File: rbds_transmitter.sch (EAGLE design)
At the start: 137 parts, among them IC1 TS974, IC2 TS974, IC3 MAX1551, IC4 MAX2606, IC5 TPS61030, IC6 MCP4812, Q1 P-CH, Q2 P-Ch, Q3 P-Ch, U1 ATMEGA328, X1 HD44780LCD-1602, Y1 16Mhz

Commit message: final design tweaks for hardware descript
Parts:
- removed ANT2: (no value), discrete:ANTENNA
- removed IC4: MAX2606, maxim:MAX2606
- removed IC6: MCP4812, microchip:MCP4812
- removed ISP1: AVRISP-6, adafruit:AVRISP-6
- removed JP1: (no value), sparkfun:M03PTH
- removed JP3, JP4: M01PTH, sparkfun:M01PTH
- removed Y1: 16Mhz, sparkfun:RESONATORSMD
- added J2: AVRISP-6, adafruit:AVRISP-6
- added LCD1: HD44780LCD-1602, adafruit:HD44780LCD-1602
- added P1: (no value), sparkfun:M03PTH
- added TP2, TP3: M01PTH, sparkfun:M01PTH
- added U5: ATMEGA328, sparkfun:ATMEGA168
- added U7: MCP4812, microchip:MCP4812
- ANT1: value (none) -> ANT; device discrete:ANTENNA -> dipole_antenna:ANT
- C1: value 1nF -> 1uF
- C10, C11: value 1uF -> 10uF
- C12: value 0.1uF -> 10uF
- C13, C14, C15: value 10uF -> 4.7uF
- C16: value 100pF -> 0.1uF
- C18, C23: value 0.1uF -> 4.7uF
- C21: value 4.7uF -> 1nF
- C22, C24: value 4.7uF -> 0.1uF
- C26, C27: value 4.7uF -> 1.5nF
- C28: value 4.7uF -> 1.2nF
- C29: value 1.396nF -> 1.2nF
- C30, C31: value 1.396nF -> 3.9nF
- C32, C33: value 1.34nF -> 3nF
- C34, C35: value 1.34nF -> 1nF
- C36: value 3.06nF -> 1uF
- C37: value 3.06nF -> 4.7uF
- C38, C39: value 3.06nF -> 1.5nF
- C40: value 100pF -> 1.2nF
- C41: value 4.188nF -> 1.2nF
- C42, C43: value 4.188nF -> 3.9nF
- C44: value 4.188nF -> 3nF
- C45: value 1.396nF -> 3nF
- L1: device rcl:L-USL1812 -> resistor:L-USL1812
- L2: value (none) -> 485nH; device resistor:L-USL1812 -> resistor:L-USL3216C
- L3: value (none) -> 10mH
- L4: value 485nH -> 6.8uH; device resistor:L-USL1812 -> rcl:L-USL1812
- R1: value 332 -> 1k
- R10, R11, R12, R14: value 2k -> 10k
- R13: value 2k -> 200
- R15: value 2k -> (none)
- R16, R17: value 2k -> 100k
- R18, R19: value 1k -> 100k
- R2, R8: value 10k -> 1k
- R20: value (none) -> 100k
- R21: value 200 -> 100k
- R24: value 100k -> 1.8M
- R25, R26, R27: value 10k -> 100k
- R28: value 10k -> 390k
- R29: value 1k -> 200k
- R3: value 10k -> 200
- R30: value 2k -> 100
- R31, R32, R33, R34, R35: value 2k -> 100k; device adafruit:R-US_R1206 -> rcl:R-TRIMM4G/J
- R36: value 2k -> 1.95M
- R37: value 1.8M -> 2k
- R38: value 390k -> 2k
- R39: value 200k -> 2k
- R40, R41, R42, R43, R44, R46, R47: value 100k -> 2k
- R45: value 100k -> 100
- R48: value 1.95M -> 2k
- R49, R50, R51, R52, R53: value 100k -> 2k; device rcl:R-TRIMM4G/J -> adafruit:R-US_R1206
- R5: value 200 -> 10k
- R9: value 2k -> 332
- U1: value ATMEGA328 -> MAX2606; device sparkfun:ATMEGA168 -> maxim:MAX2606
- X1: value HD44780LCD-1602 -> 16Mhz; device adafruit:HD44780LCD-1602 -> sparkfun:RESONATORSMD
- renumbered CN1 to J1, IC1 to U2, IC2 to U3, IC3 to U4, IC5 to U6, JP10 to TP1, JP11 to P2, JP2 to B1, JP5 to TP4, JP6 to TP5, JP7 to TP6, JP8 to TP7, JP9 to TP8, TR1 to T2, TR2 to T1
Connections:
- removed net N$15: R38.2, R48.1, U6.LBI
- new net N$27: R14.2, U7.A
- new net U7: R28.2, R36.1, U6.LBI
- net !DAC_CS: now also R10.2, U5.PD5(T1), U7.!CS; no longer IC6.!CS, R2.2, U1.PD5(T1)
- net !DAC_LATCH: now also R11.1, U5.PD6(AIN0), U7.!LDAC; no longer IC6.!LDAC, R3.1, U1.PD6(AIN0)
- net !ISP-RST: now also J2.RST, R4.1, U5.PC6(/RESET); no longer ISP1.RST, R25.1, U1.PC6(/RESET)
- net !LCD_EN: now also R17.1, U5.PD2(INT0); no longer R41.1, U1.PD2(INT0)
- net !TX_EN: now also R20.1, U5.PD1(TXD); no longer R44.1, U1.PD1(TXD)
- net +5V: now also C15.1, C20.1, C24.1, C3.1, J2.VCC, P1.3, R10.1, R16.2, R17.2, R20.2, R24.2, R4.2, U5.AREF, U5.AVCC, U5.VCC@1, U5.VCC@2; no longer C12.1, C18.1, C2.1, C28.1, ISP1.VCC, JP1.3, R2.1, R25.2, R37.2, R40.2, R41.2, R44.2, U1.AREF, U1.AVCC, U1.VCC@1, U1.VCC@2
- net AGND: now also C22.2, U5.AGND; no longer C12.2, U1.AGND
- net BPSK: now also R13.2, TP3.1; no longer JP4.1, R5.2
- net CARRIER: now also R38.2, U5.PB1(OC1A); no longer R30.2, U1.PB1(OC1A)
- net FREQUENCY: now also R21.1, TP2.1; no longer JP3.1, R45.1
- net GND: now also C13.2, C14.2, C15.2, C16.2, C3.2, C40.2, J2.GND, L2.1, LCD1.RW, LCD1.VSS, P1.1, R11.2, R12.1, R18.2, R22.2, R26.2, R28.1, R29.1, R9.1, U1.GND, U5.GND@1, U5.GND@2, U7.VSS, X1.2; no longer C1.2, C11.2, C21.2, C22.2, C34.2, C5.2, IC4.GND, IC6.VSS, ISP1.GND, JP1.1, L4.1, R1.1, R3.2, R38.1, R39.1, R4.1, R42.2, R46.2, R47.2, U1.GND@1, U1.GND@2, X1.RW, X1.VSS, Y1.2
- net ISP-MISO: now also J2.MISO, R7.2, U5.PB4(MISO); no longer ISP1.MISO, R28.2, U1.PB4(MISO)
- net ISP-MOSI: now also J2.MOSI, R6.2, U5.PB3(MOSI/OC2); no longer ISP1.MOSI, R27.2, U1.PB3(MOSI/OC2)
- net ISP-SCK: now also J2.SCK, R5.2, U5.PB5(SCK); no longer ISP1.SCK, R26.2, U1.PB5(SCK)
- net LCD0: now also LCD1.RS, U5.PC4(ADC4/SDA); no longer U1.PC4(ADC4/SDA), X1.RS
- net LCD1: now also LCD1.E, U5.PC5(ADC5/SCL); no longer U1.PC5(ADC5/SCL), X1.E
- net LCD2: now also LCD1.DB4, U5.PC0(ADC0); no longer U1.PC0(ADC0), X1.DB4
- net LCD3: now also LCD1.DB5, U5.PC1(ADC1); no longer U1.PC1(ADC1), X1.DB5
- net LCD4: now also LCD1.DB6, U5.PC2(ADC2); no longer U1.PC2(ADC2), X1.DB6
- net LCD5: now also LCD1.DB7, U5.PC3(ADC3); no longer U1.PC3(ADC3), X1.DB7
- net LOWBAT: now also R16.1, U5.PD4(XCK/T0); no longer R40.1, U1.PD4(XCK/T0)
- net MISO: now also R7.1; no longer R28.1
- net MOSI: now also R6.1, U7.SDI; no longer IC6.SDI, R27.1
- net N$1: now also C23.1, L1.2; no longer C17.1, L3.2
- net N$10: now also R15.2; no longer R20.2
- net N$11: now also C25.1, R15.1; no longer C19.1, R20.1
- net N$12: now also L4.2; no longer L1.2
- net N$17: now also R24.1, R29.2; no longer R37.1, R39.2
- net N$19: now also C12.2; no longer C15.2
- net N$2: now also U5.PB7(XTAL2/TOSC2), X1.3; no longer U1.PB7(XTAL2/TOSC2), Y1.3
- net N$20: now also C10.2; no longer C13.2
- net N$21: now also C17.1, L3.2; no longer C24.1, L2.2
- net N$22: now also R35.S; no longer R53.S
- net N$23: now also C5.1, R35.E; no longer C4.1, R53.E
- net N$24: now also L2.2, U1.IND; no longer IC4.IND, L4.2
- net N$25: now also C10.1, R13.1; no longer C13.1, R5.1
- net N$26: now also C12.1, R3.2; no longer C15.1, R21.2
- net N$28: now also U7.B; no longer IC6.B
- net N$33: now also C21.1, R30.2, U1.OUT+; no longer C40.1, IC4.OUT+, R7.2
- net N$35: now also C34.1, R45.2, U1.OUT-; no longer C16.1, IC4.OUT-, R8.2
- net N$39: now also ANT1.SIGNAL, C21.2; no longer ANT1.1, C40.2
- net N$4: now also U5.PB6(XTAL1/TOSC1), X1.1; no longer U1.PB6(XTAL1/TOSC1), Y1.1
- net N$42: now also C11.1; no longer C14.1
- net N$46: now also R12.2, R14.1; no longer IC6.A, R4.2, R6.1
- net N$5: now also C4.2, R18.1, R19.2, R35.A; no longer C3.2, R42.1, R43.2, R53.A
- net N$50: now also L4.1, R36.2; no longer L1.1, R48.2
- net N$52: now also ANT1.GND, C34.2; no longer ANT2.1, C16.2
- net N$54: now also L1.1; no longer L3.1
- net N$55: now also C27.1, R37.2, R38.1; no longer C29.1, R30.1, R31.2
- net N$59: now also C26.1, R37.1, R46.2; no longer C30.1, R31.1, R32.2
- net N$60: now also C28.1, R39.1, R48.2; no longer C33.1, R10.2, R9.1
- net N$61: now also C40.1, R48.1, R49.2; no longer C34.1, R10.1, R11.2
- net N$62: now also C41.1, R31.A, R49.1; no longer C35.1, R11.1, R49.A
- net N$63: now also C39.1, R34.A, R47.1; no longer C45.1, R36.1, R52.A
- net N$64: now also R31.S; no longer R49.S
- net N$65: now also R31.E; no longer R49.E
- net N$66: now also C2.1, R26.1, R27.2; no longer C11.1, R23.1, R24.2
- net N$67: now also C30.1, R41.1, R50.2; no longer C42.1, R12.1, R13.2
- net N$68: now also C42.1, R50.1, R51.2; no longer C43.1, R13.1, R14.2
- net N$69: now also C43.1, R32.A, R51.1; no longer C44.1, R14.1, R50.A
- net N$70: now also R32.S; no longer R50.S
- net N$71: now also R32.E; no longer R50.E
- net N$72: now also C32.1, R43.1, R52.2; no longer C37.1, R15.1, R16.2
- net N$73: now also C44.1, R52.1, R53.2; no longer C38.1, R16.1, R17.2
- net N$74: now also C45.1, R33.A, R53.1; no longer C39.1, R17.1, R51.A
- net N$75: now also R33.S; no longer R51.S
- net N$76: now also C1.1, R33.E; no longer C10.1, R51.E
- net N$77: now also R34.S; no longer R52.S
- net N$78: now also R1.2; no longer R18.2
- net N$79: now also R2.2; no longer R19.2
- net N$80: now also C1.2, R8.2; no longer C10.2, R29.2
- net N$81: now also C4.1, R1.1, R2.1, R8.1; no longer C3.1, R18.1, R19.1, R29.1
- net N$82: now also R3.1, R34.E; no longer R21.1, R52.E
- net N$83: now also C29.1, R39.2, R40.1; no longer C32.1, R33.1, R9.2
- net N$84: now also C31.1, R41.2, R42.1; no longer C41.1, R12.2, R34.1
- net N$85: now also C33.1, R43.2, R44.1; no longer C36.1, R15.2, R35.1
- net N$86: now also C38.1, R46.1, R47.2; no longer C31.1, R32.1, R36.2
- net N$9: now also LCD1.VO, R9.2; no longer R1.2, X1.VO
- net PILOT: now also R42.2, U5.PB2(SS/OC1B); no longer R34.2, U1.PB2(SS/OC1B)
- net RBDS: now also C11.2, R23.1, R25.2, R40.2; no longer C14.2, R22.2, R33.2, R47.1
- net RXD: now also P1.2, U5.PD0(RXD); no longer JP1.2, U1.PD0(RXD)
- net SCK: now also R5.1, U7.SCK; no longer IC6.SCK, R26.1
- net SIGNAL: now also C35.1, C5.2, R21.2, R22.1, U1.TUNE; no longer C1.1, C4.2, IC4.TUNE, R45.2, R46.1
- net TONE: now also R44.2, U5.PD3(INT1); no longer R35.2, U1.PD3(INT1)
- net VCC: now also C14.1, C16.1, C18.1, C19.1, C36.1, C37.1, L3.1, R19.1, R25.1, R27.1, R30.1, R45.1, U1.VCC, U7.VDD; no longer C21.1, C23.1, C25.1, C26.1, C27.1, C5.1, IC4.VCC, IC6.VDD, L2.1, R22.1, R24.1, R43.1, R6.2, R7.1, R8.1
- net VDD: now also C13.1, LCD1.VDD; no longer C20.1, X1.VDD
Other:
- note added: "J2"
- note added: "LCD1"
- note added: "P2"
- note added: "R35"
- note added: "SJ1"
- note added: "TP8"
- note added: "U2 PWR"
- note added: "U3 PWR"
- note added: "U7"
- note added: "X1"
- note removed: "IC6"
- note removed: "JP10"
- note removed: "R53"
- note removed: "Y1"
- moved on the sheet: C1, C10, C11, C12, C13, C14, C15, C16, C17, C18, C19, C2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

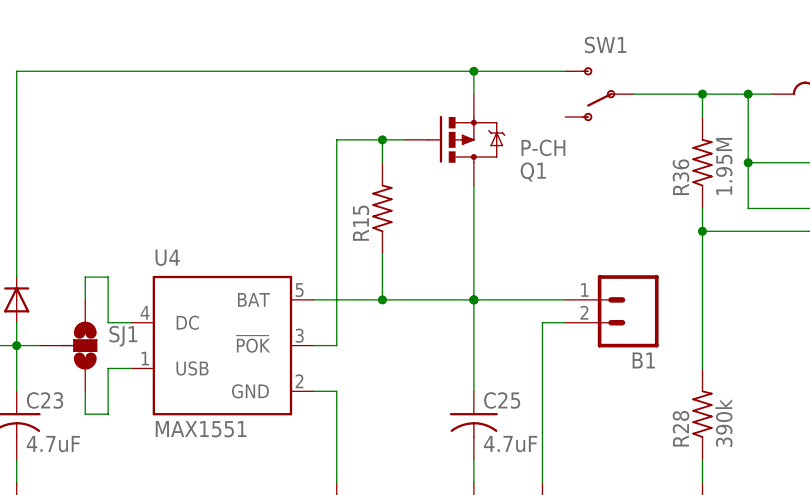
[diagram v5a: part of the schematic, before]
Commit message: added value to r15, erexported
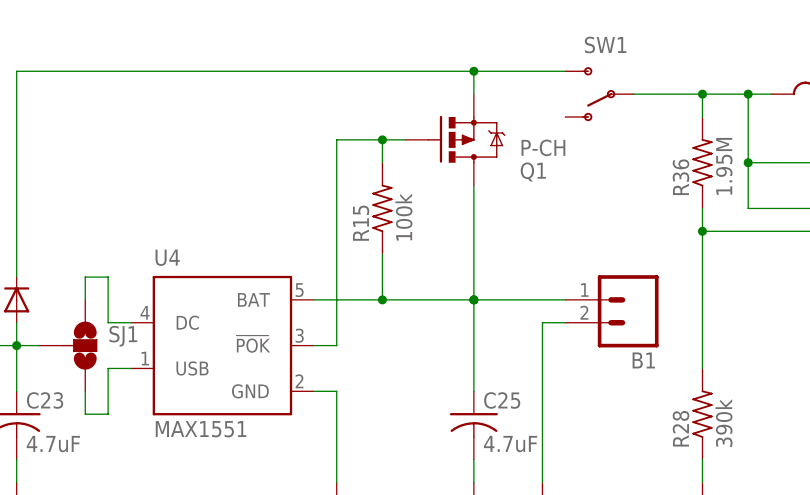
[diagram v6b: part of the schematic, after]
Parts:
- R15: value (none) -> 100k
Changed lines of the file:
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@@
 <setting verticaltext="up"/>
 </settings>
-<grid distance="0.1" unitdist="inch" unit="inch" style="lines" multiple="1" display="no" altdistance="0.05" altunitdist="inch" altunit="inch"/>
+<grid distance="0.1" unitdist="inch" unit="inch" style="lines" multiple="1" display="no" altdistance="0.01" altunitdist="inch" altunit="inch"/>
 <layers>
-<layer number="1" name="Top" color="4" fill="1" visible="yes" active="no"/>
-<layer number="2" name="Route2" color="1" fill="3" visible="yes" active="no"/>
-<layer number="3" name="Route3" color="4" fill="3" visible="yes" active="no"/>
-<layer number="4" name="Route4" color="1" fill="4" visible="yes" active="no"/>
-<layer number="5" name="Route5" color="4" fill="4" visible="yes" active="no"/>
-<layer number="6" name="Route6" color="1" fill="8" visible="yes" active="no"/>
-<layer number="7" name="Route7" color="4" fill="8" visible="yes" active="no"/>
-<layer number="8" name="Route8" color="1" fill="2" visible="yes" active="no"/>
-<layer number="9" name="Route9" color="4" fill="2" visible="yes" active="no"/>
-<layer number="10" name="Route10" color="1" fill="7" visible="yes" active="no"/>
-<layer number="11" name="Route11" color="4" fill="7" visible="yes" active="no"/>
-<layer number="12" name="Route12" color="1" fill="5" visible="yes" active="no"/>
-<layer number="13" name="Route13" color="4" fill="5" visible="yes" active="no"/>
-<layer number="14" name="Route14" color="1" fill="6" visible="yes" active="no"/>
-<layer number="15" name="Route15" color="4" fill="6" visible="yes" active="no"/>
-<layer number="16" name="Bottom" color="1" fill="1" visible="yes" active="no"/>
-<layer number="17" name="Pads" color="2" fill="1" visible="yes" active="no"/>
-<layer number="18" name="Vias" color="2" fill="1" visible="yes" active="no"/>
-<layer number="19" name="Unrouted" color="6" fill="1" visible="yes" active="no"/>
-<layer number="20" name="Dimension" color="15" fill="1" visible="yes" active="no"/>
-<layer number="21" name="tPlace" color="7" fill="1" visible="yes" active="no"/>
-<layer number="22" name="bPlace" color="7" fill="1" visible="yes" active="no"/>
-<layer number="23" name="tOrigins" color="15" fill="1" visible="yes" active="no"/>
-<layer number="24" name="bOrigins" color="15" fill="1" visible="yes" active="no"/>
-<layer number="25" name="tNames" color="7" fill="1" visible="yes" active="no"/>
-<layer number="26" name="bNames" color="7" fill="1" visible="yes" active="no"/>
-<layer number="27" name="tValues" color="7" fill="1" visible="yes" active="no"/>
-<layer number="28" name="bValues" color="7" fill="1" visible="yes" active="no"/>
+<layer number="1" name="Top" color="4" fill="1" visible="no" active="no"/>
+<layer number="2" name="Route2" color="1" fill="3" visible="no" active="no"/>
+<layer number="3" name="Route3" color="4" fill="3" visible="no" active="no"/>
+<layer number="4" name="Route4" color="1" fill="4" visible="no" active="no"/>
+<layer number="5" name="Route5" color="4" fill="4" visible="no" active="no"/>
+<layer number="6" name="Route6" color="1" fill="8" visible="no" active="no"/>
+<layer number="7" name="Route7" color="4" fill="8" visible="no" active="no"/>
+<layer number="8" name="Route8" color="1" fill="2" visible="no" active="no"/>
+<layer number="9" name="Route9" color="4" fill="2" visible="no" active="no"/>
+<layer number="10" name="Route10" color="1" fill="7" visible="no" active="no"/>
+<layer number="11" name="Route11" color="4" fill="7" visible="no" active="no"/>
+<layer number="12" name="Route12" color="1" fill="5" visible="no" active="no"/>
+<layer number="13" name="Route13" color="4" fill="5" visible="no" active="no"/>
+<layer number="14" name="Route14" color="1" fill="6" visible="no" active="no"/>
+<layer number="15" name="Route15" color="4" fill="6" visible="no" active="no"/>
+<layer number="16" name="Bottom" color="1" fill="1" visible="no" active="no"/>
+<layer number="17" name="Pads" color="2" fill="1" visible="no" active="no"/>
+<layer number="18" name="Vias" color="2" fill="1" visible="no" active="no"/>
+<layer number="19" name="Unrouted" color="6" fill="1" visible="no" active="no"/>
+<layer number="20" name="Dimension" color="15" fill="1" visible="no" active="no"/>
+<layer number="21" name="tPlace" color="7" fill="1" visible="no" active="no"/>
+<layer number="22" name="bPlace" color="7" fill="1" visible="no" active="no"/>
+<layer number="23" name="tOrigins" color="15" fill="1" visible="no" active="no"/>
+<layer number="24" name="bOrigins" color="15" fill="1" visible="no" active="no"/>
+<layer number="25" name="tNames" color="7" fill="1" visible="no" active="no"/>
+<layer number="26" name="bNames" color="7" fill="1" visible="no" active="no"/>
+<layer number="27" name="tValues" color="7" fill="1" visible="no" active="no"/>
+<layer number="28" name="bValues" color="7" fill="1" visible="no" active="no"/>
 <layer number="29" name="tStop" color="7" fill="3" visible="no" active="no"/>
 <layer number="30" name="bStop" color="7" fill="6" visible="no" active="no"/>
@@
 <layer number="35" name="tGlue" color="7" fill="4" visible="no" active="no"/>
 <layer number="36" name="bGlue" color="7" fill="5" visible="no" active="no"/>
-<layer number="37" name="tTest" color="7" fill="1" visible="yes" active="no"/>
-<layer number="38" name="bTest" color="7" fill="1" visible="yes" active="no"/>
+<layer number="37" name="tTest" color="7" fill="1" visible="no" active="no"/>
+<layer number="38" name="bTest" color="7" fill="1" visible="no" active="no"/>
 <layer number="39" name="tKeepout" color="4" fill="11" visible="no" active="no"/>
 <layer number="40" name="bKeepout" color="1" fill="11" visible="no" active="no"/>
@@
 <layer number="44" name="Drills" color="7" fill="1" visible="no" active="no"/>
 <layer number="45" name="Holes" color="7" fill="1" visible="no" active="no"/>
-<layer number="46" name="Milling" color="3" fill="1" visible="yes" active="no"/>
-<layer number="47" name="Measures" color="7" fill="1" visible="yes" active="no"/>
-<layer number="48" name="Document" color="7" fill="1" visible="yes" active="no"/>
-<layer number="49" name="Reference" color="7" fill="1" visible="yes" active="no"/>
-<layer number="50" name="dxf" color="7" fill="1" visible="yes" active="no"/>
-<layer number="51" name="tDocu" color="7" fill="1" visible="yes" active="no"/>
-<layer number="52" name="bDocu" color="7" fill="1" visible="yes" active="no"/>
-<layer number="53" name="tGND_GNDA" color="7" fill="9" visible="yes" active="no"/>
-<layer number="54" name="bGND_GNDA" color="1" fill="9" visible="yes" active="no"/>
-<layer number="56" name="wert" color="7" fill="1" visible="yes" active="no"/>
-<layer number="57" name="tCAD" color="7" fill="1" visible="yes" active="no"/>
+<layer number="46" name="Milling" color="3" fill="1" visible="no" active="no"/>
+<layer number="47" name="Measures" color="7" fill="1" visible="no" active="no"/>
+<layer number="48" name="Document" color="7" fill="1" visible="no" active="no"/>
+<layer number="49" name="Reference" color="7" fill="1" visible="no" active="no"/>
+<layer number="50" name="dxf" color="7" fill="1" visible="no" active="no"/>
+<layer number="51" name="tDocu" color="7" fill="1" visible="no" active="no"/>
+<layer number="52" name="bDocu" color="7" fill="1" visible="no" active="no"/>
+<layer number="53" name="tGND_GNDA" color="7" fill="9" visible="no" active="no"/>
+<layer number="54" name="bGND_GNDA" color="1" fill="9" visible="no" active="no"/>
+<layer number="56" name="wert" color="7" fill="1" visible="no" active="no"/>
+<layer number="57" name="tCAD" color="7" fill="1" visible="no" active="no"/>
 <layer number="91" name="Nets" color="2" fill="1" visible="yes" active="yes"/>
 <layer number="92" name="Busses" color="1" fill="1" visible="yes" active="yes"/>
@@
 <part name="Q1" library="sparkfun" deviceset="MOSFET-PCHANNEL" device="SMD" value="P-CH"/>
 <part name="D1" library="adafruit" deviceset="DIODE" device="SMA"/>
-<part name="R15" library="adafruit" deviceset="R-US_" device="R1206"/>
+<part name="R15" library="adafruit" deviceset="R-US_" device="R1206" value="100k"/>
 <part name="GND41" library="sparkfun" deviceset="GND" device=""/>
 <part name="U1" library="maxim" deviceset="MAX2606" device=""/>
